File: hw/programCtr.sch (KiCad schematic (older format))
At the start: 9 parts, among them U402 74HC10, U403 74LS191, U404 74LS191, U405 74LS191, U406 74LS191, U407 74LS541, U408 74LS541

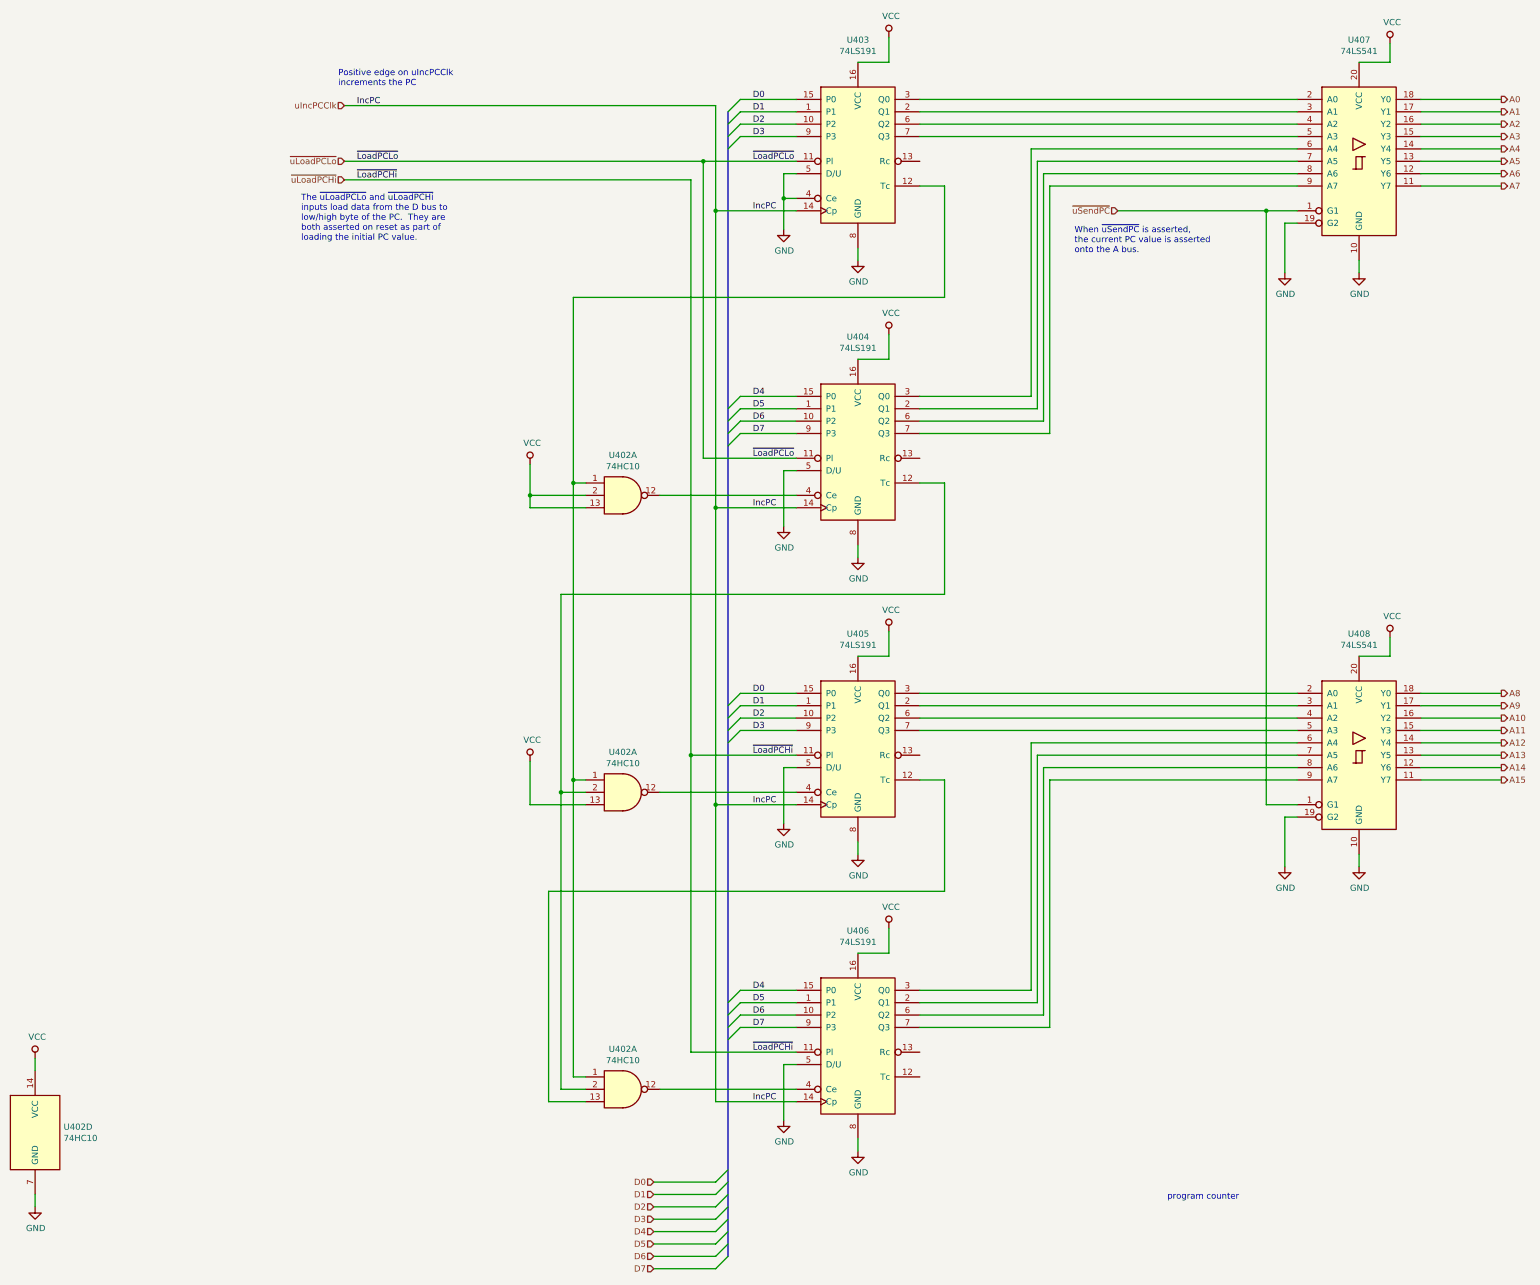
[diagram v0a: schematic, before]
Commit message: program counter is now 2x 74HCT574
Increment is done using the address generation unit,
and the output of address generation can be optionally
sent back to the address registers (such as PC)
via buffers.

This hugely simplifies the program counter implementation,
and also makes it easy to provide additional address
registers (X, SP) that can benefit from increment
and decrement operations.
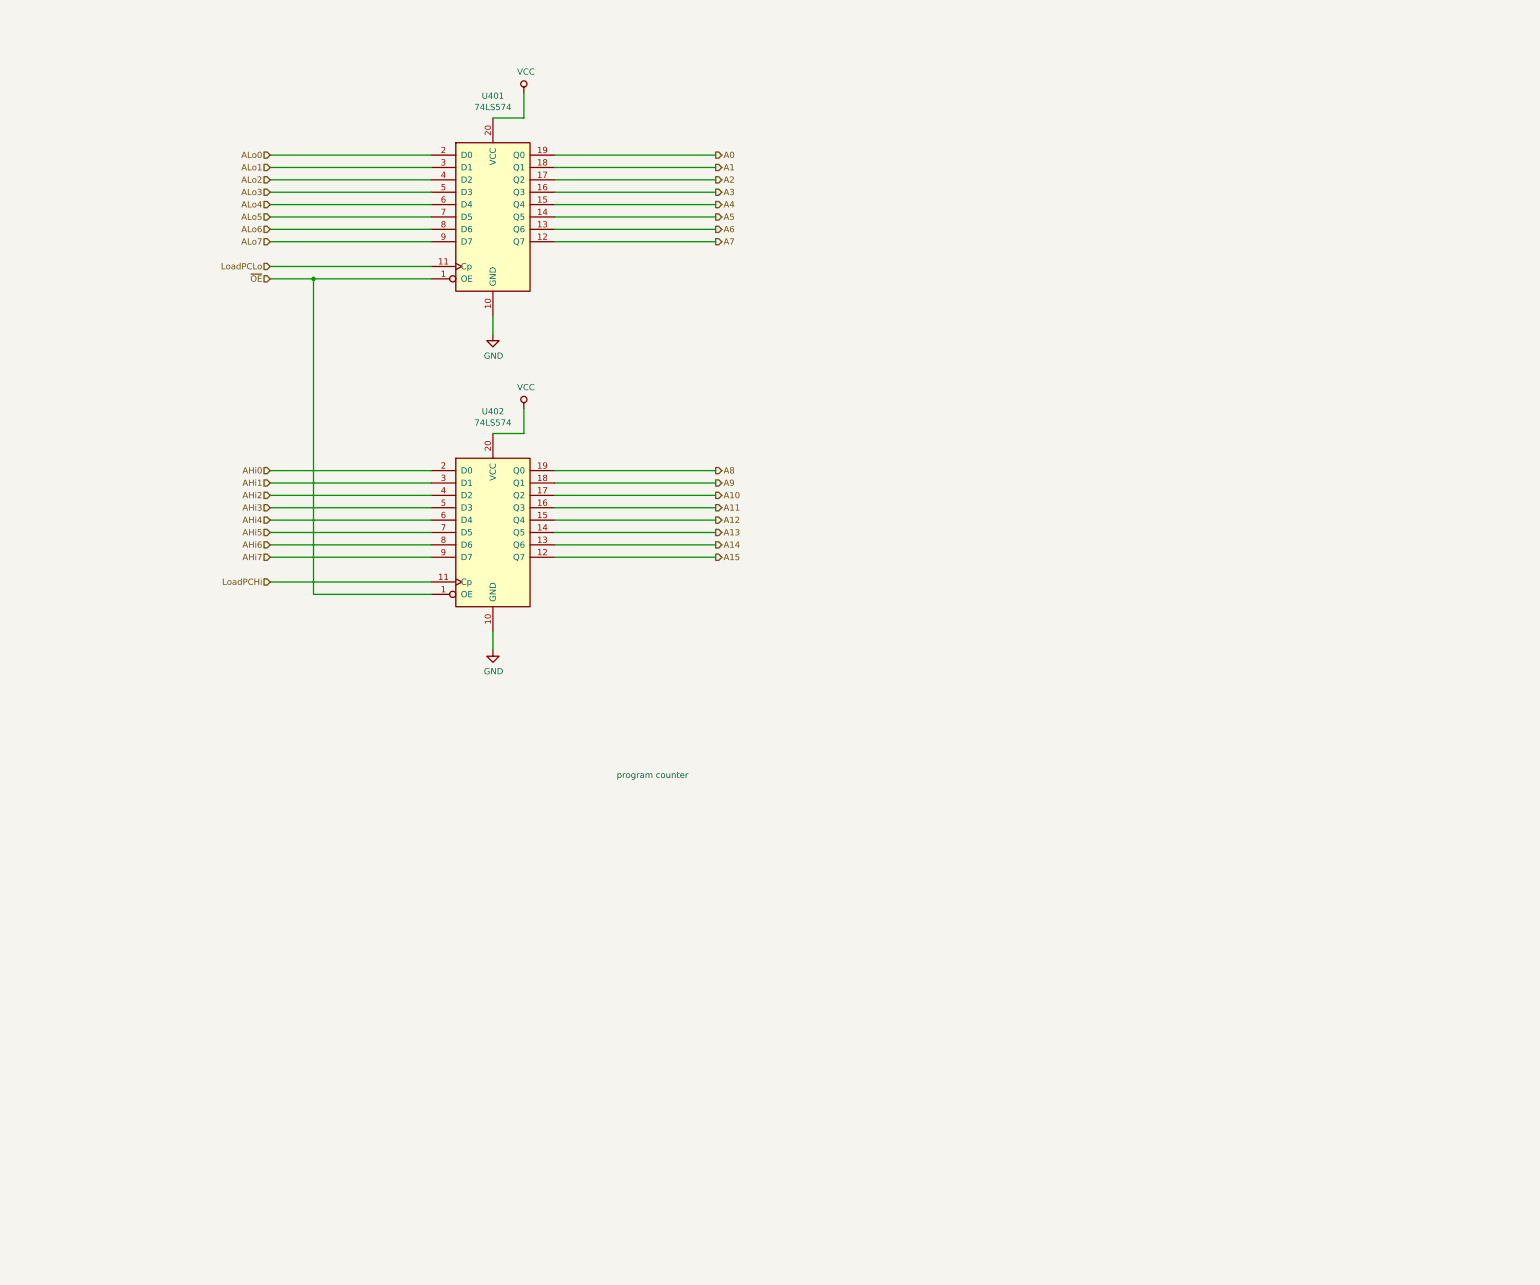
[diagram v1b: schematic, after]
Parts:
- removed U402 (x3): 74HC10, symbol 74xx:74LS10
- removed U403, U404, U405, U406: 74LS191, symbol 74xx:74LS191
- removed U407, U408: 74LS541, symbol 74xx:74LS541
- added U401, U402: 74LS574, symbol 74xx:74LS574
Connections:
- net A0: now also U401.19 (Q0)
- net A1: now also U401.18 (Q1)
- net A10: now also U402.17 (Q2)
- net A11: now also U402.16 (Q3)
- net A12: now also U402.15 (Q4)
- net A13: now also U402.14 (Q5)
- net A14: now also U402.13 (Q6)
- net A15: now also U402.12 (Q7)
- net A2: now also U401.17 (Q2)
- net A3: now also U401.16 (Q3)
- net A4: now also U401.15 (Q4)
- net A5: now also U401.14 (Q5)
- net A6: now also U401.13 (Q6)
- net A7: now also U401.12 (Q7)
- net A8: now also U402.19 (Q0)
- net A9: now also U402.18 (Q1)
- net GND: now also U401.10 (GND), U402.10 (GND)
- net VCC: now also U401.20 (VCC), U402.20 (VCC)
- new net AHi0: U402.2 (D0)
- new net AHi1: U402.3 (D1)
- new net AHi2: U402.4 (D2)
- new net AHi3: U402.5 (D3)
- new net AHi4: U402.6 (D4)
- new net AHi5: U402.7 (D5)
- new net AHi6: U402.8 (D6)
- new net AHi7: U402.9 (D7)
- new net ALo0: U401.2 (D0)
- new net ALo1: U401.3 (D1)
- new net ALo2: U401.4 (D2)
- new net ALo3: U401.5 (D3)
- new net ALo4: U401.6 (D4)
- new net ALo5: U401.7 (D5)
- new net ALo6: U401.8 (D6)
- new net ALo7: U401.9 (D7)
- new net LoadPCHi: U402.11 (Cp)
- new net LoadPCLo: U401.11 (Cp)
- new net ~OE: U401.1 (OE), U402.1 (OE)
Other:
- note removed: "Positive edge on uIncPCClk\nincrements the PC"
- note removed: "The ~uLoadPCLo~ and ~uLoadPCHi~\ninputs load data from the D bus to\nlow/high byte of the PC. They are\nboth asserted on reset as part of\nloading the initial PC value."
- note removed: "When ~uSendPC~ is asserted,\nthe current PC value is asserted\nonto the A bus."
